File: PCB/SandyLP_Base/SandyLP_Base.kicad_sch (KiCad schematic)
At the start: 180 parts, among them J1 Conn_01x10_Pin, J7 USB_C_Receptacle_USB2.0, J8 Conn_01x03, Q1 BSS138, SW1 BOOT, SW2 RESET, U1 NCP1117-3.3_SOT223, U2 RP2040, U3 W25Q128JVPIQ, Y1 12MHz

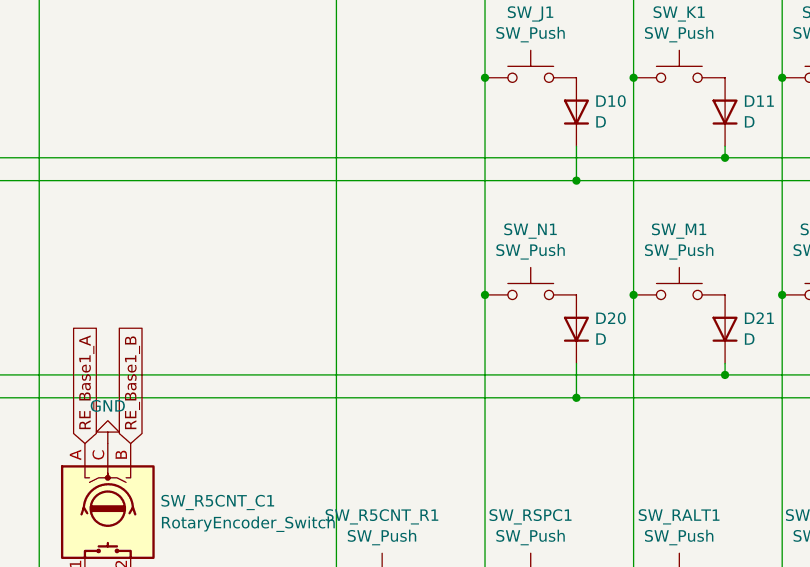
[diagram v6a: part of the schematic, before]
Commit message: マトリクスの未使用部分のメモを追加
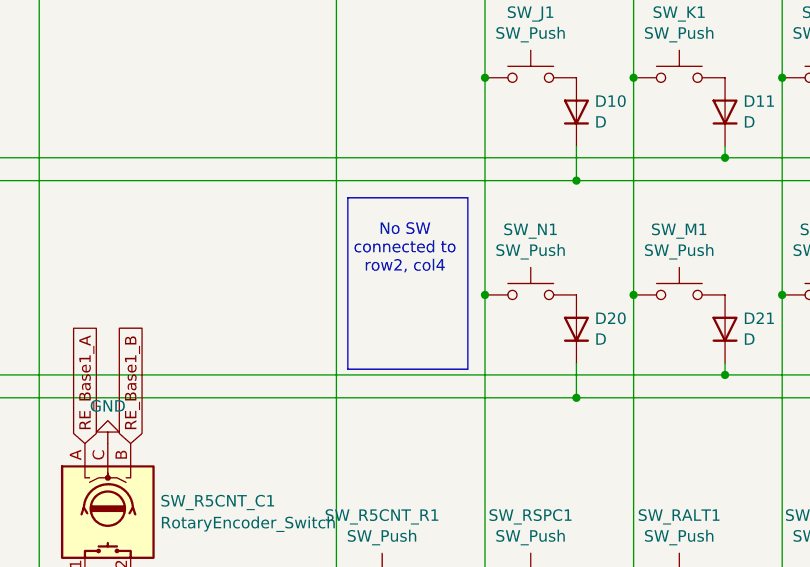
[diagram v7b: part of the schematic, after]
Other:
- note added: "No SW connected to row2, col4"
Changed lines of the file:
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@@
+		)
+	)
+	(rectangle
+		(start 156.21 83.185)
+		(end 169.545 102.235)
+		(stroke
+			(width 0)
+			(type default)
+		)
+		(fill
+			(type none)
 		)
 	)
@@
 		)
 	)
+	(text "No SW\nconnected to\nrow2, col4"
+		(exclude_from_sim no)
+		(at 162.56 88.9 0)
+		(effects
+			(font
+				(size 1.27 1.27)
+			)
+		)
+	)

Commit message: シルク追加。ロゴのフットプリント指定を修正。
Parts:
- LOGO1: footprint locallib:SandyLP_logo_w60 -> locallib:SandyLP_logo_LP40_w60
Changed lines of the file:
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@@
 			)
 		)
-		(property "Footprint" "locallib:SandyLP_logo_w60"
+		(property "Footprint" "locallib:SandyLP_logo_LP40_w60"
 			(at 251.46 27.305 0)
 			(effects
